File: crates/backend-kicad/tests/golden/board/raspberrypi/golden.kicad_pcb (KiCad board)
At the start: 2 copper layers, 100 x 80 mm, 3 parts, among them U1 U

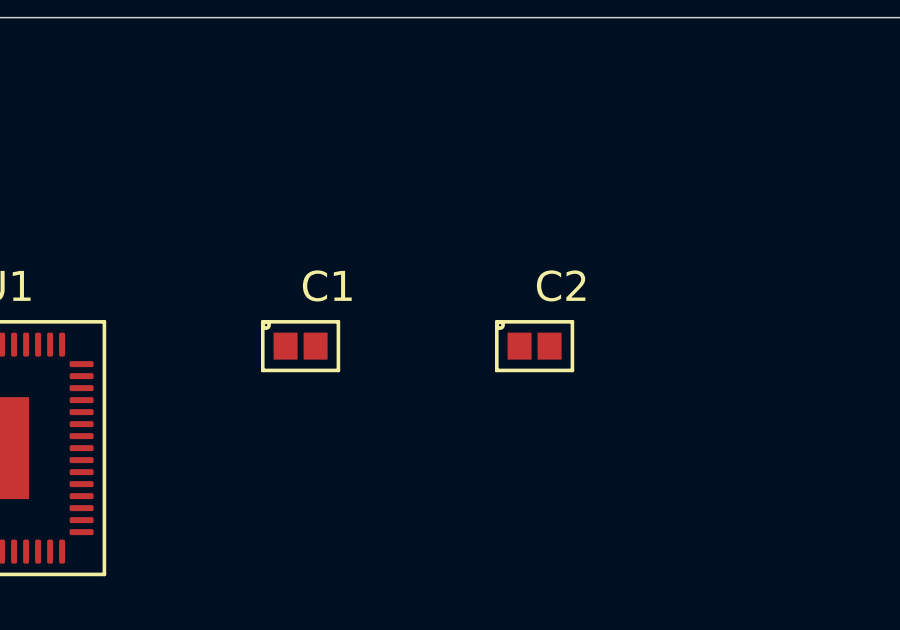
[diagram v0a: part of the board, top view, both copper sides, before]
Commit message: Fix bugs with footprints and DRC rules
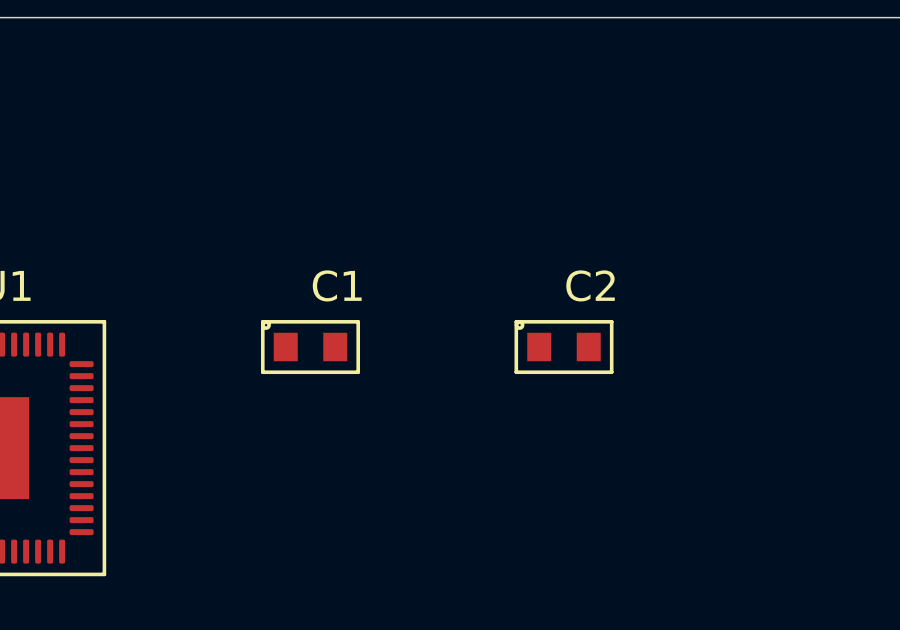
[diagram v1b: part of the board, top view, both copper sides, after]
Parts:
- moved C2 0.98 mm to (33.9, 11.0)
- moved C1 0.33 mm to (25.4, 11.0)
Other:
- net class Default: trace_width 0.25 -> 0.2
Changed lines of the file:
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@@
   (net_class "Default" ""
     (clearance 0.2)
-    (trace_width 0.25)
+    (trace_width 0.2)
     (via_dia 0.8)
     (via_drill 0.4)
@@
     (layer "F.Cu")
     (locked no)
-    (at 25.1 10.95 0)
+    (at 25.43 10.98 0)
     (property "Reference" "C1"
-      (at 0 -1.97 0)
+      (at 0 -2 0)
       (layer "F.SilkS")
       (effects
@@
         (justify left)))
     (property "Value" "C"
-      (at 0 1.97 0)
+      (at 0 2 0)
       (layer "F.SilkS")
       (hide yes)
@@
         (justify left)))
     (fp_text user "${VALUE}"
-      (at 0 1.97)
+      (at 0 2)
       (layer F.Fab)
       (effects
@@
     (attr smd)
     (fp_line
-      (start -1.15 -0.7)
-      (end 1.15 -0.7)
-      (layer F.Fab)
-      (width 0.1)
-)
-    (fp_line
-      (start 1.15 -0.7)
-      (end 1.15 0.7)
-      (layer F.Fab)
-      (width 0.1)
-)
-    (fp_line
-      (start 1.15 0.7)
-      (end -1.15 0.7)
-      (layer F.Fab)
-      (width 0.1)
-)
-    (fp_line
-      (start -1.15 0.7)
-      (end -1.15 -0.7)
-      (layer F.Fab)
-      (width 0.1)
-)
-    (fp_line
-      (start -1.26 -0.81)
-      (end 1.26 -0.81)
-      (layer F.SilkS)
-      (width 0.12)
-)
-    (fp_line
-      (start 1.26 -0.81)
-      (end 1.26 0.81)
-      (layer F.SilkS)
-      (width 0.12)
-)
-    (fp_line
-      (start 1.26 0.81)
-      (end -1.26 0.81)
-      (layer F.SilkS)
-      (width 0.12)
-)
-    (fp_line
-      (start -1.26 0.81)
-      (end -1.26 -0.81)
-      (layer F.SilkS)
-      (width 0.12)
-)
-    (fp_line
-      (start -1.4 -0.95)
-      (end 1.4 -0.95)
-      (layer F.CrtYd)
-      (width 0.05)
-)
-    (fp_line
-      (start 1.4 -0.95)
-      (end 1.4 0.95)
-      (layer F.CrtYd)
-      (width 0.05)
-)
-    (fp_line
-      (start 1.4 0.95)
-      (end -1.4 0.95)
-      (layer F.CrtYd)
-      (width 0.05)
-)
-    (fp_line
-      (start -1.4 0.95)
-      (end -1.4 -0.95)
+      (start -1.48 -0.73)
+      (end 1.48 -0.73)
+      (layer F.Fab)
+      (width 0.1)
+)
+    (fp_line
+      (start 1.48 -0.73)
+      (end 1.48 0.73)
+      (layer F.Fab)
+      (width 0.1)
+)
+    (fp_line
+      (start 1.48 0.73)
+      (end -1.48 0.73)
+      (layer F.Fab)
+      (width 0.1)
+)
+    (fp_line
+      (start -1.48 0.73)
+      (end -1.48 -0.73)
+      (layer F.Fab)
+      (width 0.1)
+)
+    (fp_line
+      (start -1.59 -0.84)
+      (end 1.59 -0.84)
+      (layer F.SilkS)
+      (width 0.12)
+)
+    (fp_line
+      (start 1.59 -0.84)
+      (end 1.59 0.84)
+      (layer F.SilkS)
+      (width 0.12)
+)
+    (fp_line
+      (start 1.59 0.84)
+      (end -1.59 0.84)
+      (layer F.SilkS)
+      (width 0.12)
+)
+    (fp_line
+      (start -1.59 0.84)
+      (end -1.59 -0.84)
+      (layer F.SilkS)
+      (width 0.12)
+)
+    (fp_line
+      (start -1.73 -0.98)
+      (end 1.73 -0.98)
+      (layer F.CrtYd)
+      (width 0.05)
+)
+    (fp_line
+      (start 1.73 -0.98)
+      (end 1.73 0.98)
+      (layer F.CrtYd)
+      (width 0.05)
+)
+    (fp_line
+      (start 1.73 0.98)
+      (end -1.73 0.98)
+      (layer F.CrtYd)
+      (width 0.05)
+)
+    (fp_line
+      (start -1.73 0.98)
+      (end -1.73 -0.98)
       (layer F.CrtYd)
       (width 0.05)
 )
     (fp_circle
-      (center -1.15 -0.7)
-      (end -1.05 -0.7)
+      (center -1.48 -0.73)
+      (end -1.38 -0.73)
       (layer F.SilkS)
       (width 0.12)
 )
     (pad "1" smd rect
-      (at -0.5 0)
-      (size 0.8 0.9)
+      (at -0.825 0)
+      (size 0.8 0.95)
       (layers F.Cu F.Mask F.Paste)
       (net 1 "NET_U1_ADC_AVDD"))
     (pad "2" smd rect
-      (at 0.5 0)
-      (size 0.8 0.9)
+      (at 0.825 0)
+      (size 0.8 0.95)
       (layers F.Cu F.Mask F.Paste)
       (net 2 "NET_U1_VREG_PGND"))
@@
     (layer "F.Cu")
     (locked no)
-    (at 32.9 10.95 0)
+    (at 33.88 10.98 0)
     (property "Reference" "C2"
-      (at 0 -1.97 0)
+      (at 0 -2 0)
       (layer "F.SilkS")
       (effects
@@
         (justify left)))
     (property "Value" "C"
-      (at 0 1.97 0)
+      (at 0 2 0)
       (layer "F.SilkS")
       (hide yes)
@@
         (justify left)))
     (fp_text user "${VALUE}"
-      (at 0 1.97)
+      (at 0 2)
       (layer F.Fab)
       (effects
@@
     (attr smd)
     (fp_line
-      (start -1.15 -0.7)
-      (end 1.15 -0.7)
-      (layer F.Fab)
-      (width 0.1)
-)
-    (fp_line
-      (start 1.15 -0.7)
-      (end 1.15 0.7)
-      (layer F.Fab)
-      (width 0.1)
-)
-    (fp_line
-      (start 1.15 0.7)
-      (end -1.15 0.7)
-      (layer F.Fab)
-      (width 0.1)
-)
-    (fp_line
-      (start -1.15 0.7)
-      (end -1.15 -0.7)
-      (layer F.Fab)
-      (width 0.1)
-)
-    (fp_line
-      (start -1.26 -0.81)
-      (end 1.26 -0.81)
-      (layer F.SilkS)
-      (width 0.12)
-)
-    (fp_line
-      (start 1.26 -0.81)
-      (end 1.26 0.81)
-      (layer F.SilkS)
-      (width 0.12)
-)
-    (fp_line
-      (start 1.26 0.81)
-      (end -1.26 0.81)
-      (layer F.SilkS)
-      (width 0.12)
-)
-    (fp_line
-      (start -1.26 0.81)
-      (end -1.26 -0.81)
-      (layer F.SilkS)
-      (width 0.12)
-)
-    (fp_line
-      (start -1.4 -0.95)
-      (end 1.4 -0.95)
-      (layer F.CrtYd)
-      (width 0.05)
-)
-    (fp_line
-      (start 1.4 -0.95)
-      (end 1.4 0.95)
-      (layer F.CrtYd)
-      (width 0.05)
-)
-    (fp_line
-      (start 1.4 0.95)
-      (end -1.4 0.95)
-      (layer F.CrtYd)
-      (width 0.05)
-)
-    (fp_line
-      (start -1.4 0.95)
-      (end -1.4 -0.95)
+      (start -1.48 -0.73)
+      (end 1.48 -0.73)
+      (layer F.Fab)
+      (width 0.1)
+)
+    (fp_line
+      (start 1.48 -0.73)
+      (end 1.48 0.73)
+      (layer F.Fab)
+      (width 0.1)
+)
+    (fp_line
+      (start 1.48 0.73)
+      (end -1.48 0.73)
+      (layer F.Fab)
+      (width 0.1)
+)
+    (fp_line
+      (start -1.48 0.73)
+      (end -1.48 -0.73)
+      (layer F.Fab)
+      (width 0.1)
+)
+    (fp_line
+      (start -1.59 -0.84)
+      (end 1.59 -0.84)
+      (layer F.SilkS)
+      (width 0.12)
+)
+    (fp_line
+      (start 1.59 -0.84)
+      (end 1.59 0.84)
+      (layer F.SilkS)
+      (width 0.12)
+)
+    (fp_line
+      (start 1.59 0.84)
+      (end -1.59 0.84)
+      (layer F.SilkS)
+      (width 0.12)
+)
+    (fp_line
+      (start -1.59 0.84)
+      (end -1.59 -0.84)
+      (layer F.SilkS)
+      (width 0.12)
+)
+    (fp_line
+      (start -1.73 -0.98)
+      (end 1.73 -0.98)
+      (layer F.CrtYd)
+      (width 0.05)
+)
+    (fp_line
+      (start 1.73 -0.98)
+      (end 1.73 0.98)
+      (layer F.CrtYd)
+      (width 0.05)
+)
+    (fp_line
+      (start 1.73 0.98)
+      (end -1.73 0.98)
+      (layer F.CrtYd)
+      (width 0.05)
+)
+    (fp_line
+      (start -1.73 0.98)
+      (end -1.73 -0.98)
       (layer F.CrtYd)
       (width 0.05)
 )
     (fp_circle
-      (center -1.15 -0.7)
-      (end -1.05 -0.7)
+      (center -1.48 -0.73)
+      (end -1.38 -0.73)
       (layer F.SilkS)
       (width 0.12)
 )
     (pad "1" smd rect
-      (at -0.5 0)
-      (size 0.8 0.9)
+      (at -0.825 0)
+      (size 0.8 0.95)
       (layers F.Cu F.Mask F.Paste)
       (net 1 "NET_U1_ADC_AVDD"))
     (pad "2" smd rect
-      (at 0.5 0)
-      (size 0.8 0.9)
+      (at 0.825 0)
+      (size 0.8 0.95)
       (layers F.Cu F.Mask F.Paste)
       (net 2 "NET_U1_VREG_PGND"))
